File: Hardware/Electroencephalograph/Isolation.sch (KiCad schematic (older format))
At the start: 21 parts, among them U4 THI3-0511, U5 ADUM2401BRWZ

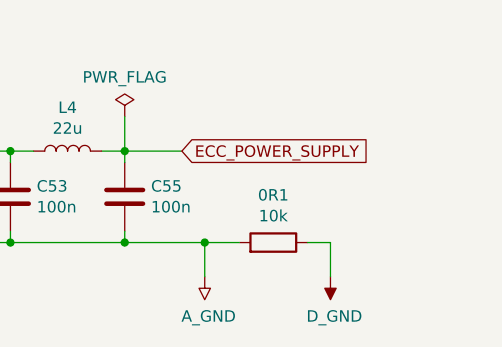
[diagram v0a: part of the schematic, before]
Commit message: add bom
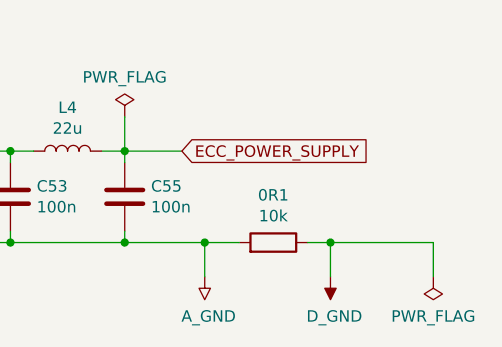
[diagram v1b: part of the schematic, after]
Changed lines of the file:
@@
 Wire Wire Line
 	5500 5200 5600 5200
+$Comp
+L power:PWR_FLAG #FLG0105
+U 1 1 60DE084C
+P 6050 5350
+F 0 "#FLG0105" H 6050 5425 50  0001 C CNN
+F 1 "PWR_FLAG" H 6050 5523 50  0000 C CNN
+F 2 "" H 6050 5350 50  0001 C CNN
+F 3 "~" H 6050 5350 50  0001 C CNN
+	1    6050 5350
+	-1   0    0    1
+$EndComp
+Wire Wire Line
+	6050 5200 6050 5350
+Wire Wire Line
+	5600 5200 6050 5200
+Connection ~ 5600 5200
 $EndSCHEMATC
